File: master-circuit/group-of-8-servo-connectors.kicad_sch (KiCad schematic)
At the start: 6 parts

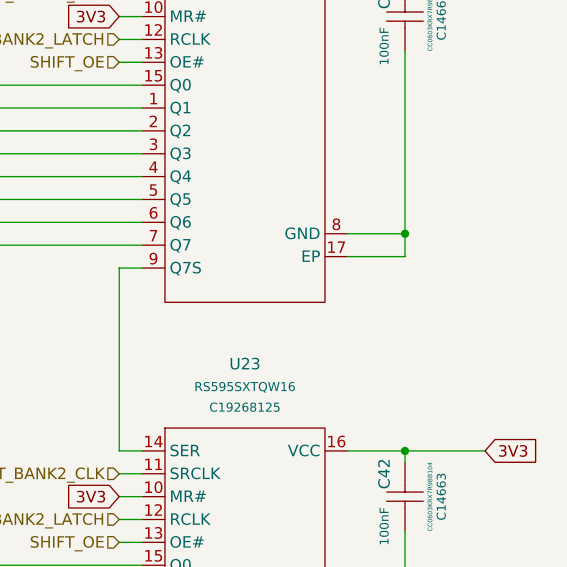
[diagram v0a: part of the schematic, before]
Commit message: Almost wired controller.
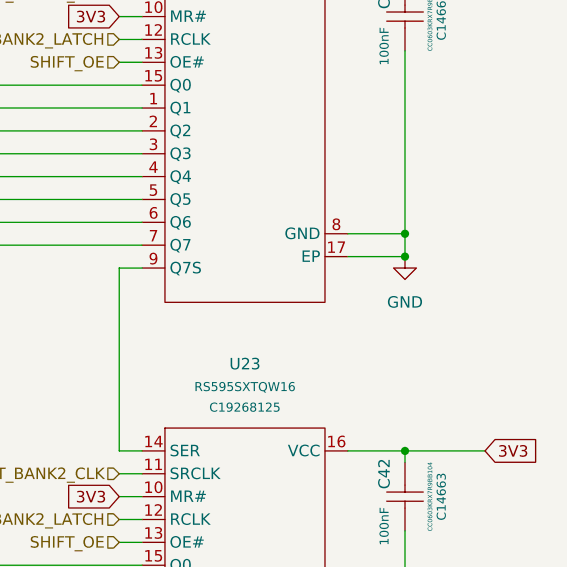
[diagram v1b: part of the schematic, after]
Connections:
- net GND: now also C41.1, U22.17 (EP), U22.8 (GND)
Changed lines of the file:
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@@
+	)
+	(junction
+		(at 261.62 68.58)
+		(diameter 0)
+		(color 0 0 0 0)
 	)
 	(junction
@@
 					(unit 1)
 				)
+			)
+		)
+	)
+	(symbol
+		(lib_id "power:GND")
+		(at 261.62 68.58 0)
+		(mirror y)
+		(unit 1)
+		(exclude_from_sim no)
+		(in_bom yes)
+		(on_board yes)
+		(dnp no)
+		(property "Reference" "#PWR073"
+			(at 261.62 74.93 0)
+			(effects
+				(font
+					(size 1.27 1.27)
+				)
+				(hide yes)
+			)
+		)
+		(property "Value" "GND"
+			(at 261.62 73.66 0)
+			(effects
+				(font
+					(size 1.27 1.27)
+				)
+			)
+		)
+		(property "Footprint" ""
+			(at 261.62 68.58 0)
+			(effects
+				(font
+					(size 1.27 1.27)
+				)
+				(hide yes)
+			)
+		)
+		(property "Datasheet" ""
+			(at 261.62 68.58 0)
+			(effects
+				(font
+					(size 1.27 1.27)
+				)
+				(hide yes)
+			)
+		)
+		(property "Description" "Power symbol creates a global label with name \"GND\" , ground"
+			(at 261.62 68.58 0)
+			(effects
+				(font
+					(size 1.27 1.27)
+				)
+				(hide yes)
+			)
+		)
+		(pin "1"
+		)
+		(instances
+			(project "master-circuit"
+				(path "/240d81ac-e9d7-42ea-a748-33df14683b07/07dd894a-a677-4867-9a80-03490d776b7d"
+					(reference "#PWR074")
+					(unit 1)
+				)
+				(path "/240d81ac-e9d7-42ea-a748-33df14683b07/1de2ebe0-3144-4ba5-879d-b7b7f508a713"
+					(reference "#PWR075")
+					(unit 1)
+				)
+				(path "/240d81ac-e9d7-42ea-a748-33df14683b07/e5556145-7a45-4d81-bcd4-6b93a85b8194"
+					(reference "#PWR073")
+					(unit 1)
+				)
